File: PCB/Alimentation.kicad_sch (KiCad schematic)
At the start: 2 parts, among them J1 Conn_01x02

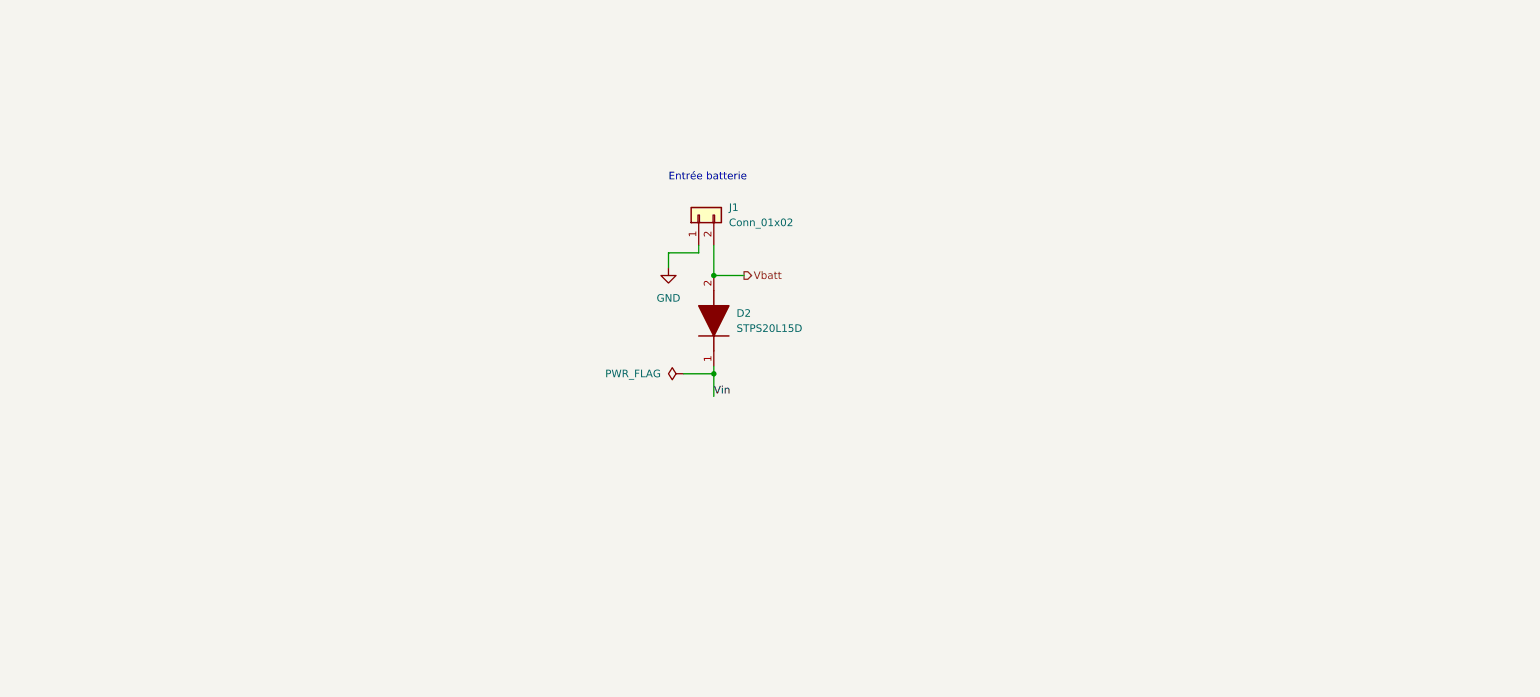
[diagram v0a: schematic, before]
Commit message: List of Modifs:
Corrected power supply sheet
Updated motor driver sheet
Added a project name to a lot of sheets (don't know why...)
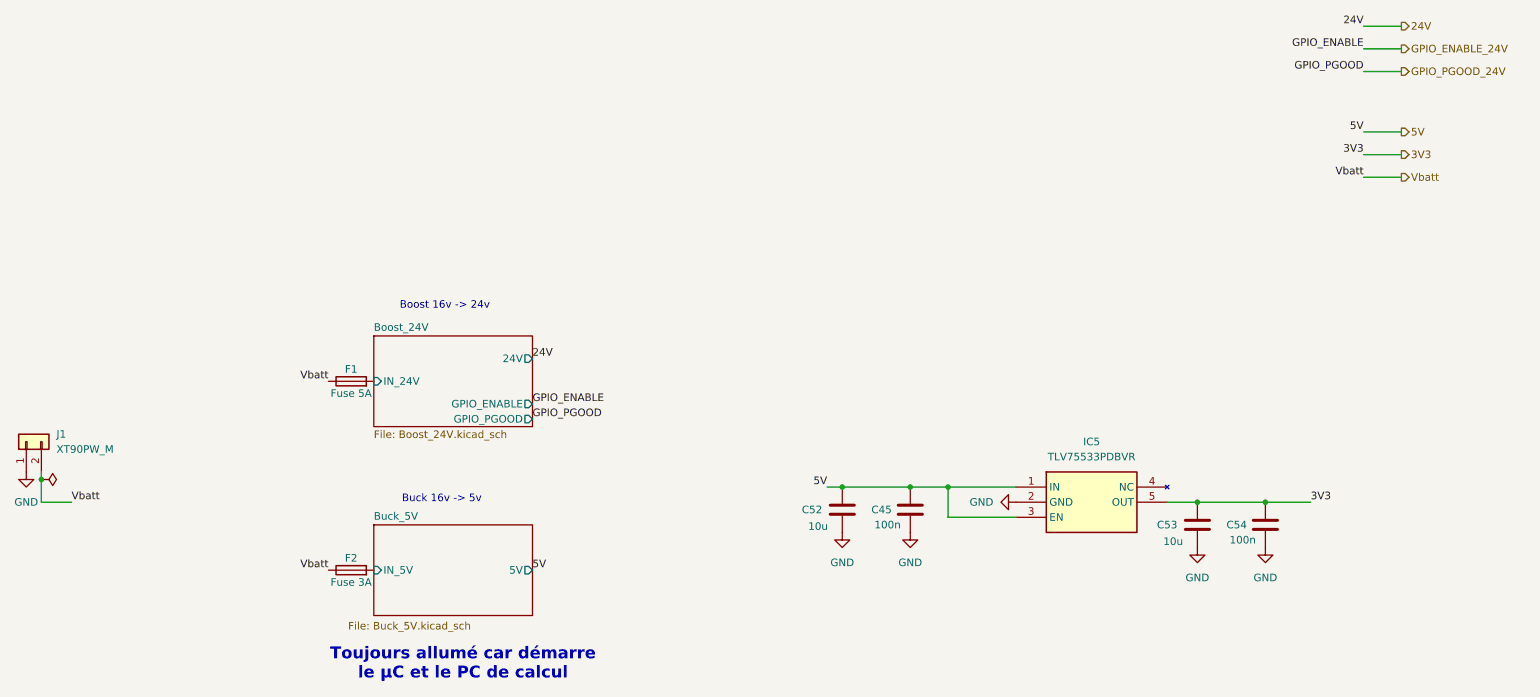
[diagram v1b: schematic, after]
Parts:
- removed D2: STPS20L15D, TO515P460X1020X2008-2P, symbol SamacSys_Parts:STPS20L15D
- added C45, C54: 100n, symbol Device:C
- added C52, C53: 10u, symbol Device:C
- added F1: Fuse 5A, symbol Device:Fuse
- added F2: Fuse 3A, symbol Device:Fuse
- added IC5: TLV75533PDBVR, SOT95P280X145-5N, symbol SamacSys_new:TLV75533PDBVR
- J1: value Conn_01x02 -> XT90PW_M; footprint (none) -> Connector_AMASS:AMASS_XT90PW-M_1x02_P10.90mm_Horizontal; Manufacturer_Part_Number (none) -> XT90PW-M
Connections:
- net GND: now also C45.2, C52.2, C53.2, C54.2, IC5.2 (GND)
- net Vbatt: now also F1.1, F2.1
- new net 3V3: C53.1, C54.1, IC5.5 (OUT)
- new net 5V: C45.1, C52.1, IC5.1 (IN), IC5.3 (EN)
- new net Boost_24V/IN_24V: F1.2
- new net Buck_5V/IN_5V: F2.2
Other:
- added sheet Boost_24V (Boost_24V.kicad_sch)
- added sheet Buck_5V (Buck_5V.kicad_sch)
- note added: "Boost 16v -> 24v"
- note added: "Buck 16v -> 5v"
- note added: "Toujours allumé car démarre le µC et le PC de calcul"
- note removed: "Entrée batterie"
- moved on the sheet: J1
